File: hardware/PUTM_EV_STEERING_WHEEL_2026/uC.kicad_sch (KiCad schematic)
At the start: 8 parts, among them U1 STM32G0C1KCTxN

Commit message: Preview schematic
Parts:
- added C1: 10u, Capacitor_SMD:C_0603_1608Metric_Pad1.08x0.95mm_HandSolder, symbol Device:C_Small
- added C2, C4: 100n, Capacitor_SMD:C_0603_1608Metric_Pad1.08x0.95mm_HandSolder, symbol Device:C_Small
- added C3, C5: 4u7, Capacitor_SMD:C_0603_1608Metric_Pad1.08x0.95mm_HandSolder, symbol Device:C_Small
- added R1: 0, Resistor_SMD:R_0603_1608Metric_Pad0.98x0.95mm_HandSolder, symbol Device:R_Small
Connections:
- net +3V3: now also R1.1
- net GND: now also C1.2, C2.2, C3.2, C4.2, C5.2
- net LED_CAN: now also U1.17 (PB15); no longer U1.31 (PB7)
- net TX: now reaches U1.30 (PB6)
- net POWER renamed STM_VCC
- net STM_VCC: now also C1.1, C2.1, C3.1, C4.1, C5.1, R1.2
- new net RX: U1.31 (PB7)
- no-connect marks 17 -> 16
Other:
- moved on the sheet: D1, D2, D3, R2, R3, R4

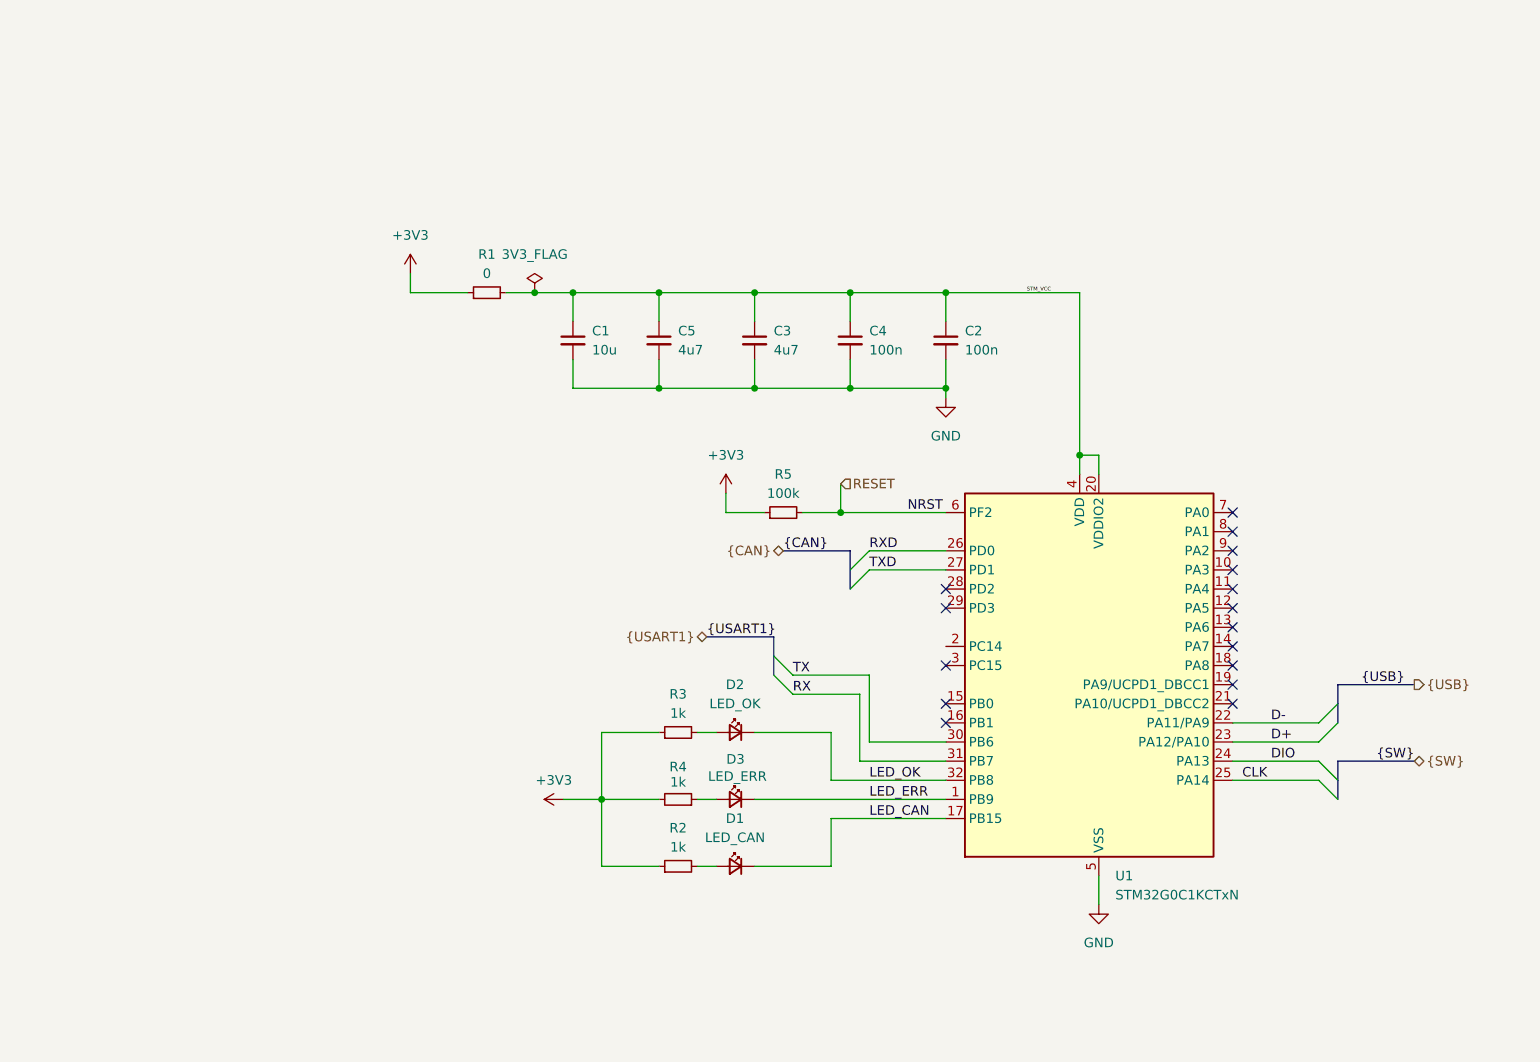
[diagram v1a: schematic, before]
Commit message: Edit MCU G0->G4, add RS in schema
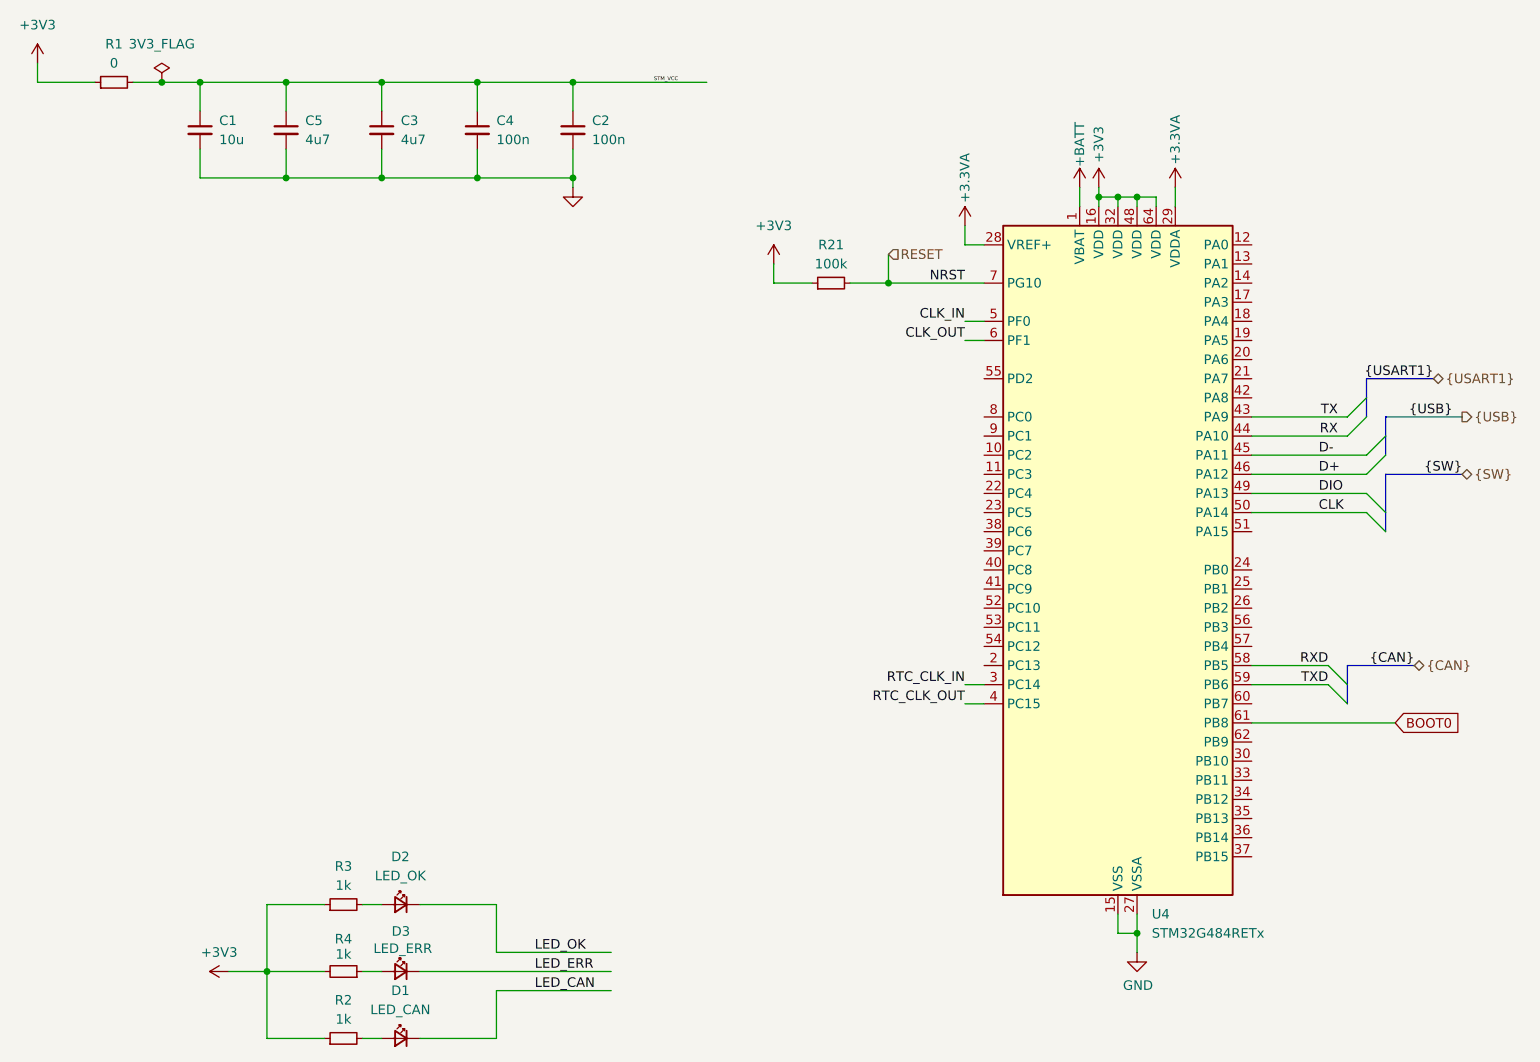
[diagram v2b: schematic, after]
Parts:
- removed R5: 100k, Resistor_SMD:R_0603_1608Metric_Pad0.98x0.95mm_HandSolder, symbol Device:R_Small
- removed U1: STM32G0C1KCTxN, Package_QFP:LQFP-32_7x7mm_P0.8mm, symbol MCU_ST_STM32G0:STM32G0C1KCTxN
- added R21: 100k, Resistor_SMD:R_0603_1608Metric_Pad0.98x0.95mm_HandSolder, symbol Device:R_Small
- added U4: STM32G484RETx, Package_QFP:LQFP-64_10x10mm_P0.5mm, symbol MCU_ST_STM32G4:STM32G484RETx
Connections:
- net +3V3: now also R21.1, U4.16 (VDD), U4.32 (VDD), U4.48 (VDD), U4.64 (VDD)
- net CLK: now also U4.50 (PA14)
- net D+: now also U4.46 (PA12)
- net D-: now also U4.45 (PA11)
- net DIO: now also U4.49 (PA13)
- net GND: now also U4.15 (VSS), U4.27 (VSSA), U4.31 (VSS), U4.47 (VSS), U4.63 (VSS)
- net RESET: now also R21.2, U4.7 (PG10)
- net RX: now also U4.44 (PA10)
- net RXD: now also U4.58 (PB5)
- net TX: now also U4.43 (PA9)
- net TXD: now also U4.59 (PB6)
- new net +3.3VA: U4.28 (VREF+), U4.29 (VDDA)
- new net +BATT: U4.1 (VBAT)
- new net BOOT0: U4.61 (PB8)
- new net CLK_IN: U4.5 (PF0)
- new net CLK_OUT: U4.6 (PF1)
- new net RTC_CLK_IN: U4.3 (PC14)
- new net RTC_CLK_OUT: U4.4 (PC15)
- no-connect marks 16 -> 0
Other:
- moved on the sheet: C1, C2, C3, C4, C5, D1, D2, D3, R1, R2, R3, R4
